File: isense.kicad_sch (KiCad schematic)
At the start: 21 parts, among them U1 TLV2372, U7 INA138, U8 LM2904, U9 LM393LV

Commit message: Fix ground references
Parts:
- added C19: 0.1u, symbol Device:C
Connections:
- net +3.3VA: now also C19.2
- net GNDPWR: now also C19.1
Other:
- moved on the sheet: R14, R15, R16, R17, R18, R19, R20, R21, U9A, U9B, U9C

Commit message: formatting!?!? idk what I changed tbh
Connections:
- no-connect marks 0 -> 2
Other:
- note added: "V_{TH}"
- note added: "V_{TL}"

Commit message: Updating symbol library + passing some ERC tests
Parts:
- U4: renamed from U9; symbol ! Robomaster:LM393LV -> ! Robomaster ICs:LM393LV
- renumbered C19 to C2, R6 to R1, R16 to R10, R17 to R11, R15 to R12, R18 to R13, R19 to R14, R20 to R15, R21 to R16, R4 to R2, R5 to R3, R12 to R4, R13 to R5, R7 to R6, R2 to R7, R3 to R8, R14 to R9, U7 to U1, U1 to U2, U8 to U3

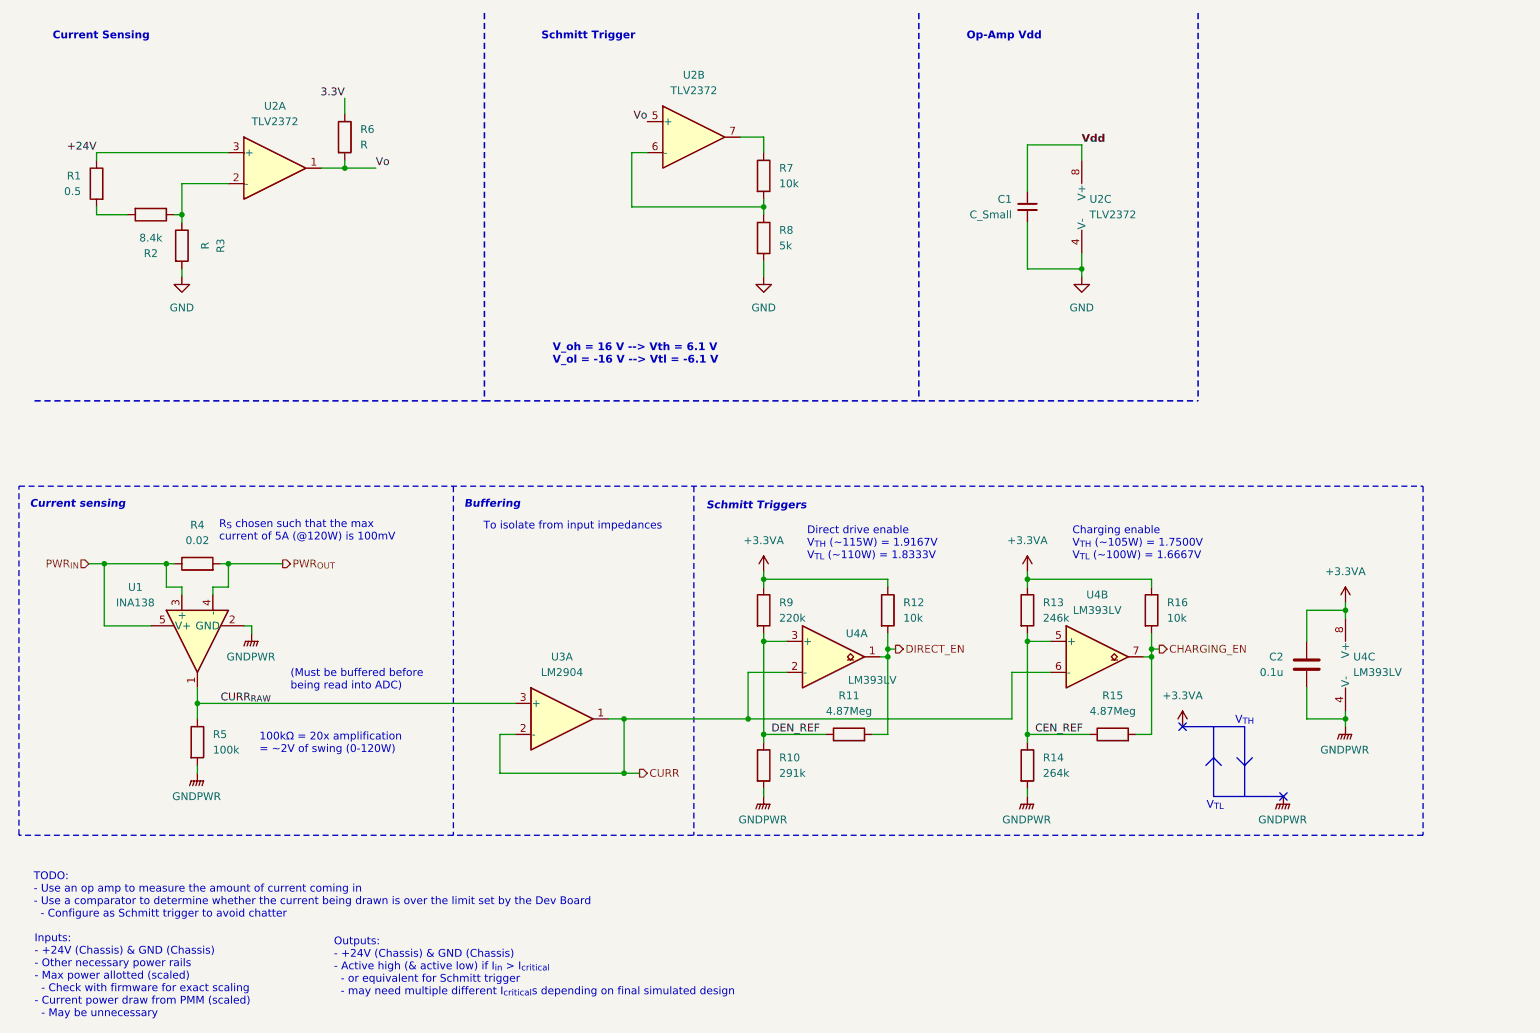
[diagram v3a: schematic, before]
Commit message: Remove previous version of current sense
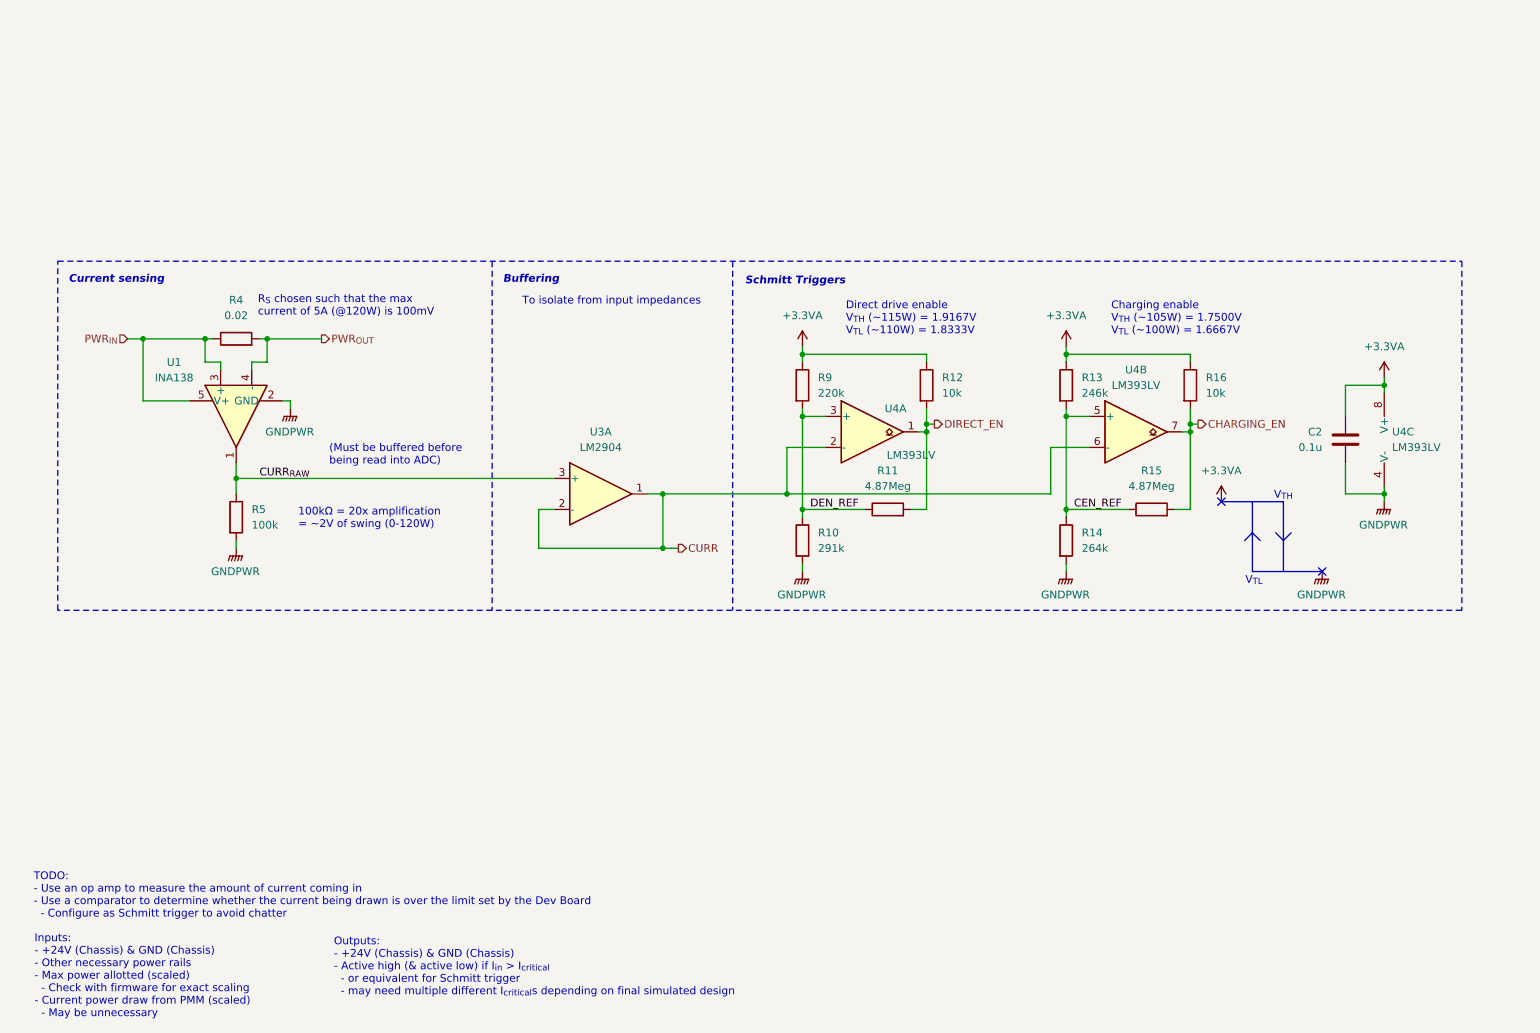
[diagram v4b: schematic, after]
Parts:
- removed C1: C_Small, symbol Device:C_Small
- removed R1: 0.5, symbol Device:R
- removed R2: 8.4k, symbol Device:R
- removed R3, R6: R, symbol Device:R
- removed R7: 10k, symbol Device:R
- removed R8: 5k, symbol Device:R
- removed U2: TLV2372, symbol Amplifier_Operational:TLV2372
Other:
- note removed: "Current Sensing"
- note removed: "Op-Amp Vdd"
- note removed: "Schmitt Trigger"
- note removed: "V_oh = 16 V --> Vth = 6.1 V V_ol = -16 V --> Vtl = -6.1 V"
- moved on the sheet: C2, R10, R11, R12, R13, R14, R15, R16, R4, R5, R9, U1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

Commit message: Add input resistor divider to battery voltage ADC
+ renumbered components
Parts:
- renumbered C2 to C1, R4 to R1, R16 to R10, R5 to R2, R9 to R3, R10 to R4, R11 to R5, R12 to R6, R13 to R7, R14 to R8, R15 to R9, U3 to U2, U4 to U3
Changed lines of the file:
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@@
 		(dnp no)
 		(fields_autoplaced yes)
-		(property "Reference" "R4"
+		(property "Reference" "R1"
 			(at 63.5 72.39 90)
 			(effects
@@
 			(project ""
 				(path "/6197145b-e7d4-44cc-9d90-537b6501bf60/9739d4cc-938e-4869-b5d8-561f0e1056cb"
-					(reference "R4")
+					(reference "R1")
 					(unit 1)
 				)
@@
 		(dnp no)
 		(fields_autoplaced yes)
-		(property "Reference" "U4"
+		(property "Reference" "U3"
 			(at 210.82 83.82 0)
 			(effects
@@
 			(project ""
 				(path "/6197145b-e7d4-44cc-9d90-537b6501bf60/9739d4cc-938e-4869-b5d8-561f0e1056cb"
-					(reference "U4")
+					(reference "U3")
 					(unit 2)
 				)
@@
 		(dnp no)
 		(fields_autoplaced yes)
-		(property "Reference" "#PWR020"
+		(property "Reference" "#PWR017"
 			(at 251.46 88.9 0)
 			(effects
@@
 			(project ""
 				(path "/6197145b-e7d4-44cc-9d90-537b6501bf60/9739d4cc-938e-4869-b5d8-561f0e1056cb"
-					(reference "#PWR020")
+					(reference "#PWR017")
 					(unit 1)
 				)
@@
 		(dnp no)
 		(fields_autoplaced yes)
-		(property "Reference" "#PWR018"
+		(property "Reference" "#PWR015"
 			(at 224.79 109.22 0)
 			(effects
@@
 			(project "SupercapManager"
 				(path "/6197145b-e7d4-44cc-9d90-537b6501bf60/9739d4cc-938e-4869-b5d8-561f0e1056cb"
-					(reference "#PWR018")
+					(reference "#PWR015")
 					(unit 1)
 				)
@@
 		(dnp no)
 		(fields_autoplaced yes)
-		(property "Reference" "R9"
+		(property "Reference" "R3"
 			(at 158.75 85.0899 0)
 			(effects
@@
 			(project ""
 				(path "/6197145b-e7d4-44cc-9d90-537b6501bf60/9739d4cc-938e-4869-b5d8-561f0e1056cb"
-					(reference "R9")
+					(reference "R3")
 					(unit 1)
 				)
@@
 		(dnp no)
 		(fields_autoplaced yes)
-		(property "Reference" "#PWR015"
+		(property "Reference" "#PWR013"
 			(at 199.39 83.82 0)
 			(effects
@@
 			(project "SupercapManager"
 				(path "/6197145b-e7d4-44cc-9d90-537b6501bf60/9739d4cc-938e-4869-b5d8-561f0e1056cb"
-					(reference "#PWR015")
+					(reference "#PWR013")
 					(unit 1)
 				)
@@
 		(dnp no)
 		(fields_autoplaced yes)
-		(property "Reference" "R13"
+		(property "Reference" "R7"
 			(at 201.93 85.0899 0)
 			(effects
@@
 			(project "SupercapManager"
 				(path "/6197145b-e7d4-44cc-9d90-537b6501bf60/9739d4cc-938e-4869-b5d8-561f0e1056cb"
-					(reference "R13")
+					(reference "R7")
 					(unit 1)
 				)
@@
 		(dnp no)
 		(fields_autoplaced yes)
-		(property "Reference" "#PWR021"
+		(property "Reference" "#PWR018"
 			(at 251.46 110.49 0)
 			(effects
@@
 			(project ""
 				(path "/6197145b-e7d4-44cc-9d90-537b6501bf60/9739d4cc-938e-4869-b5d8-561f0e1056cb"
-					(reference "#PWR021")
+					(reference "#PWR018")
 					(unit 1)
 				)
@@
 		(dnp no)
 		(fields_autoplaced yes)
-		(property "Reference" "C2"
+		(property "Reference" "C1"
 			(at 241.3 93.9799 0)
 			(effects
@@
 			(project "SupercapManager"
 				(path "/6197145b-e7d4-44cc-9d90-537b6501bf60/9739d4cc-938e-4869-b5d8-561f0e1056cb"
-					(reference "C2")
+					(reference "C1")
 					(unit 1)
 				)
@@
 		(dnp no)
 		(fields_autoplaced yes)
-		(property "Reference" "R15"
+		(property "Reference" "R9"
 			(at 213.36 100.33 90)
 			(effects
@@
 			(project "SupercapManager"
 				(path "/6197145b-e7d4-44cc-9d90-537b6501bf60/9739d4cc-938e-4869-b5d8-561f0e1056cb"
-					(reference "R15")
+					(reference "R9")
 					(unit 1)
 				)
@@
 		(dnp no)
 		(fields_autoplaced yes)
-		(property "Reference" "R10"
+		(property "Reference" "R4"
 			(at 158.75 110.4899 0)
 			(effects
@@
 			(project "SupercapManager"
 				(path "/6197145b-e7d4-44cc-9d90-537b6501bf60/9739d4cc-938e-4869-b5d8-561f0e1056cb"
-					(reference "R10")
+					(reference "R4")
 					(unit 1)
 				)
@@
 		(dnp no)
 		(fields_autoplaced yes)
-		(property "Reference" "#PWR013"
+		(property "Reference" "#PWR011"
 			(at 156.21 83.82 0)
 			(effects
@@
 			(project "SupercapManager"
 				(path "/6197145b-e7d4-44cc-9d90-537b6501bf60/9739d4cc-938e-4869-b5d8-561f0e1056cb"
-					(reference "#PWR013")
+					(reference "#PWR011")
 					(unit 1)
 				)
@@
 		(dnp no)
 		(fields_autoplaced yes)
-		(property "Reference" "R5"
+		(property "Reference" "R2"
 			(at 66.04 106.6799 0)
 			(effects
@@
 			(project ""
 				(path "/6197145b-e7d4-44cc-9d90-537b6501bf60/9739d4cc-938e-4869-b5d8-561f0e1056cb"
-					(reference "R5")
+					(reference "R2")
 					(unit 1)
 				)
@@
 		(dnp no)
 		(fields_autoplaced yes)
-		(property "Reference" "R14"
+		(property "Reference" "R8"
 			(at 201.93 110.4899 0)
 			(effects
@@
 			(project "SupercapManager"
 				(path "/6197145b-e7d4-44cc-9d90-537b6501bf60/9739d4cc-938e-4869-b5d8-561f0e1056cb"
-					(reference "R14")
+					(reference "R8")
 					(unit 1)
 				)
@@
 		(dnp no)
 		(fields_autoplaced yes)
-		(property "Reference" "U4"
+		(property "Reference" "U3"
 			(at 252.73 93.9799 0)
 			(effects
@@
 			(project ""
 				(path "/6197145b-e7d4-44cc-9d90-537b6501bf60/9739d4cc-938e-4869-b5d8-561f0e1056cb"
-					(reference "U4")
+					(reference "U3")
 					(unit 3)
 				)
@@
 		(dnp no)
 		(fields_autoplaced yes)
-		(property "Reference" "#PWR014"
+		(property "Reference" "#PWR012"
 			(at 156.21 121.92 0)
 			(effects
@@
 			(project "SupercapManager"
 				(path "/6197145b-e7d4-44cc-9d90-537b6501bf60/9739d4cc-938e-4869-b5d8-561f0e1056cb"
-					(reference "#PWR014")
+					(reference "#PWR012")
 					(unit 1)
 				)
@@
 		(dnp no)
 		(fields_autoplaced yes)
-		(property "Reference" "R11"
+		(property "Reference" "R5"
 			(at 170.18 100.33 90)
 			(effects
@@
 			(project "SupercapManager"
 				(path "/6197145b-e7d4-44cc-9d90-537b6501bf60/9739d4cc-938e-4869-b5d8-561f0e1056cb"
-					(reference "R11")
+					(reference "R5")
 					(unit 1)
 				)
@@
 		(dnp no)
 		(fields_autoplaced yes)
-		(property "Reference" "#PWR016"
+		(property "Reference" "#PWR014"
 			(at 199.39 121.92 0)
 			(effects
@@
 			(project "SupercapManager"
 				(path "/6197145b-e7d4-44cc-9d90-537b6501bf60/9739d4cc-938e-4869-b5d8-561f0e1056cb"
-					(reference "#PWR016")
+					(reference "#PWR014")
 					(unit 1)
 				)
@@
 		(dnp no)
 		(fields_autoplaced yes)
-		(property "Reference" "#PWR010"
+		(property "Reference" "#PWR09"
 			(at 63.5 118.11 0)
 			(effects
@@
 			(project "SupercapManager"
 				(path "/6197145b-e7d4-44cc-9d90-537b6501bf60/9739d4cc-938e-4869-b5d8-561f0e1056cb"
-					(reference "#PWR010")
+					(reference "#PWR09")
 					(unit 1)
 				)
@@
 		(dnp no)
 		(fields_autoplaced yes)
-		(property "Reference" "#PWR019"
+		(property "Reference" "#PWR016"
 			(at 241.3 121.92 0)
 			(effects
@@
 			(project "SupercapManager"
 				(path "/6197145b-e7d4-44cc-9d90-537b6501bf60/9739d4cc-938e-4869-b5d8-561f0e1056cb"
-					(reference "#PWR019")
+					(reference "#PWR016")
 					(unit 1)
 				)
@@
 		(dnp no)
 		(fields_autoplaced yes)
-		(property "Reference" "R12"
+		(property "Reference" "R6"
 			(at 179.07 85.0899 0)
 			(effects
@@
 			(project "SupercapManager"
 				(path "/6197145b-e7d4-44cc-9d90-537b6501bf60/9739d4cc-938e-4869-b5d8-561f0e1056cb"
-					(reference "R12")
+					(reference "R6")
 					(unit 1)
 				)
@@
 		(dnp no)
 		(fields_autoplaced yes)
-		(property "Reference" "#PWR011"
+		(property "Reference" "#PWR010"
 			(at 72.39 95.25 0)
 			(effects
@@
 			(project ""
 				(path "/6197145b-e7d4-44cc-9d90-537b6501bf60/9739d4cc-938e-4869-b5d8-561f0e1056cb"
-					(reference "#PWR011")
+					(reference "#PWR010")
 					(unit 1)
 				)
@@
 		(on_board yes)
 		(dnp no)
-		(property "Reference" "U4"
+		(property "Reference" "U3"
 			(at 171.45 90.17 0)
 			(effects
@@
 			(project ""
 				(path "/6197145b-e7d4-44cc-9d90-537b6501bf60/9739d4cc-938e-4869-b5d8-561f0e1056cb"
-					(reference "U4")
+					(reference "U3")
 					(unit 1)
 				)
@@
 		(dnp no)
 		(fields_autoplaced yes)
-		(property "Reference" "R16"
+		(property "Reference" "R10"
 			(at 222.25 85.0899 0)
 			(effects
@@
 			(project "SupercapManager"
 				(path "/6197145b-e7d4-44cc-9d90-537b6501bf60/9739d4cc-938e-4869-b5d8-561f0e1056cb"
-					(reference "R16")
+					(reference "R10")
 					(unit 1)
 				)
@@
 		(dnp no)
 		(fields_autoplaced yes)
-		(property "Reference" "U3"
+		(property "Reference" "U2"
 			(at 123.19 93.98 0)
 			(effects
@@
 			(project ""
 				(path "/6197145b-e7d4-44cc-9d90-537b6501bf60/9739d4cc-938e-4869-b5d8-561f0e1056cb"
-					(reference "U3")
-					(unit 1)
-				)
+					(reference "U2")
+					(unit 1)
+				)

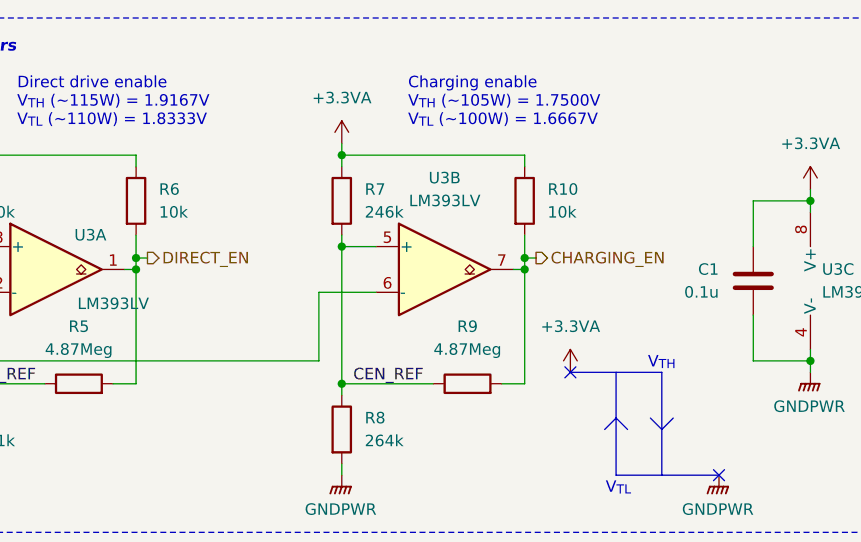
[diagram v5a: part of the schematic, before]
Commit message: Add in voltage control for components
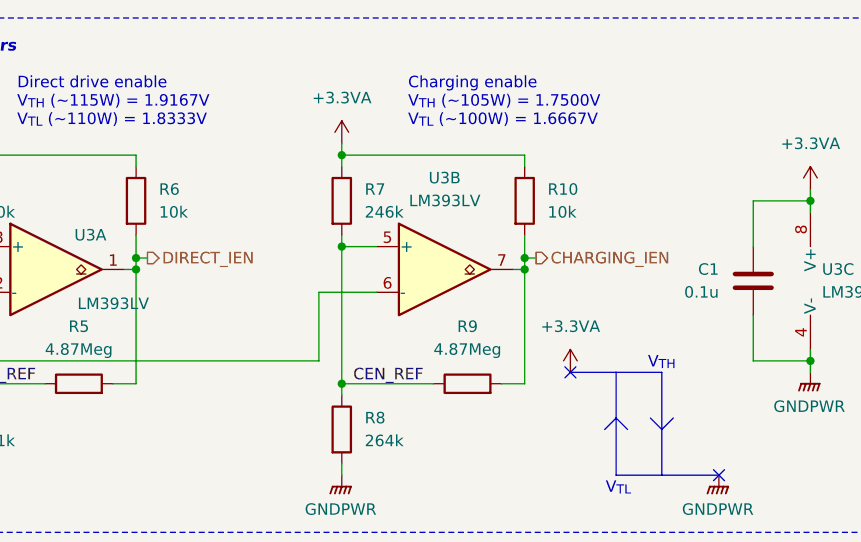
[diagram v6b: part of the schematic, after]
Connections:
- net CHARGING_EN renamed CHARGING_IEN
- net DIRECT_EN renamed DIRECT_IEN
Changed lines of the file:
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@@
 		)
 	)
-	(hierarchical_label "DIRECT_EN"
+	(hierarchical_label "DIRECT_IEN"
 		(shape output)
 		(at 177.8 92.71 0)
@@
 		)
 	)
-	(hierarchical_label "CHARGING_EN"
+	(hierarchical_label "CHARGING_IEN"
 		(shape output)
 		(at 220.98 92.71 0)

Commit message: Finish up buck
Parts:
- C1: footprint (none) -> Capacitor_SMD:C_0603_1608Metric_Pad1.08x0.95mm_HandSolder
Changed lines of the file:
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@@
 			)
 		)
-		(property "Footprint" ""
+		(property "Footprint" "Capacitor_SMD:C_0603_1608Metric_Pad1.08x0.95mm_HandSolder"
 			(at 246.0752 91.44 0)
 			(effects

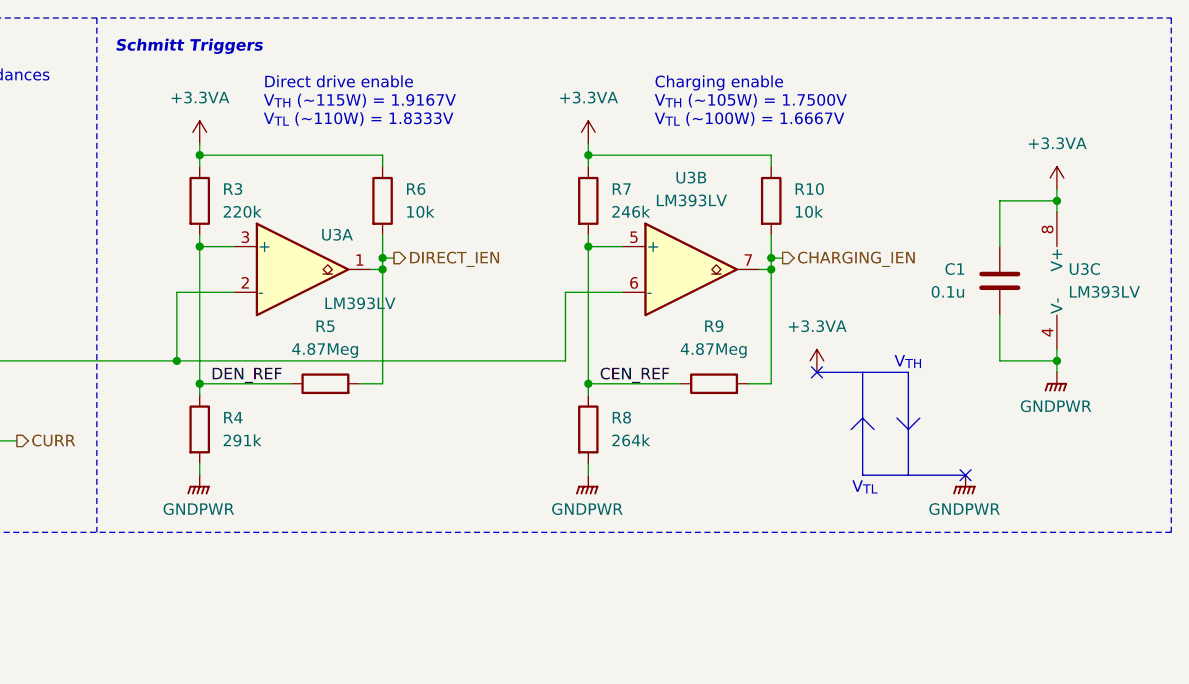
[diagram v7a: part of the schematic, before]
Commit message: Add global connectors
Also realize I messed up the current sense
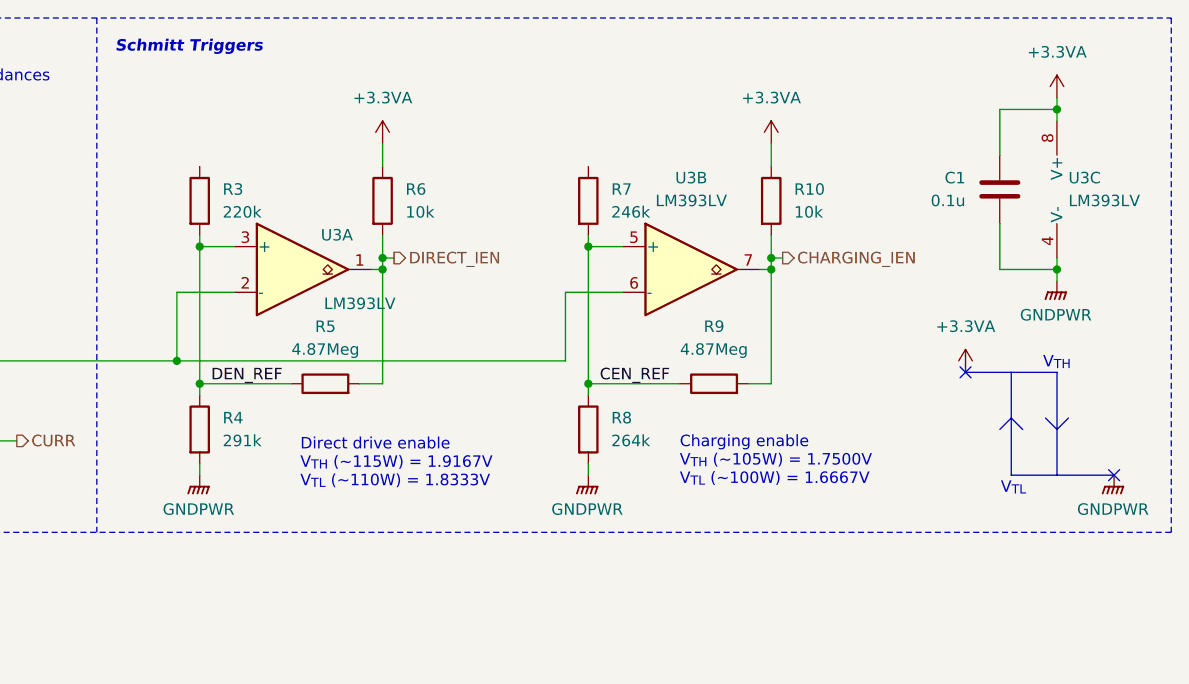
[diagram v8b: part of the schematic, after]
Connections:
- net +3.3VA: no longer R3.1, R7.1
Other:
- moved on the sheet: C1, U3C
